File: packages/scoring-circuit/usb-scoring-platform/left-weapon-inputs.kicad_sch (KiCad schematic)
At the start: 15 parts, among them J3 LEFT WEAPON A B C, U8 SN74LVC125APWR

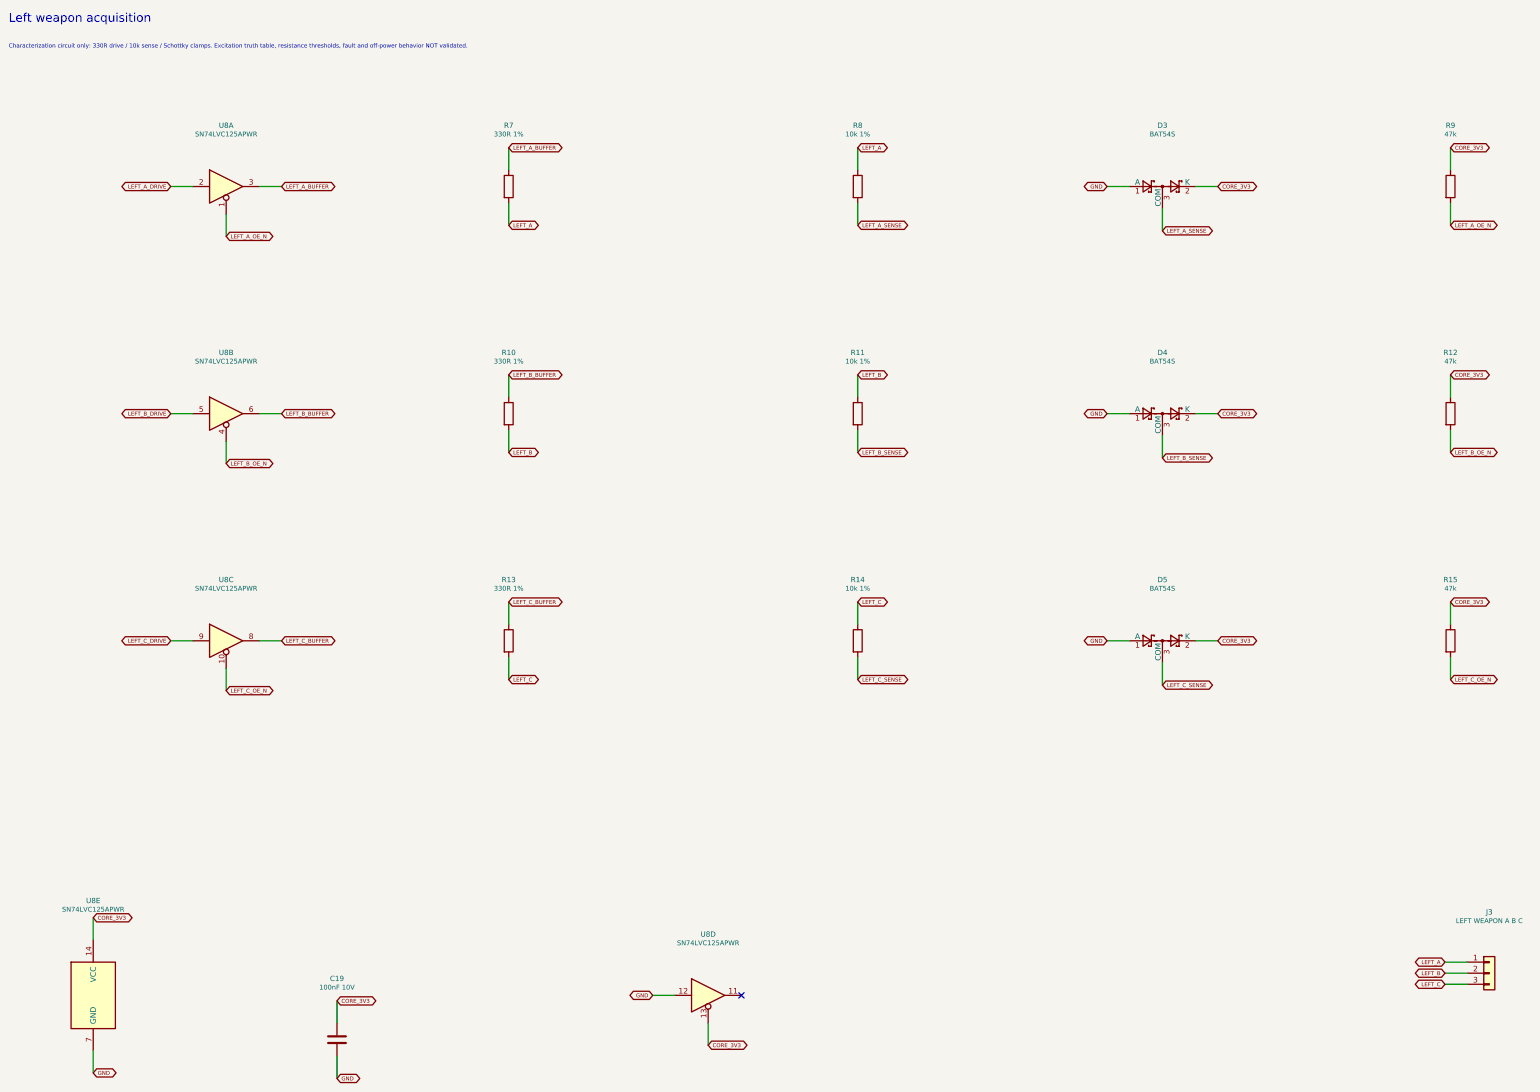
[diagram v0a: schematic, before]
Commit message: fix(scoring-circuit): strengthen STM32 sensing bias and model continuity
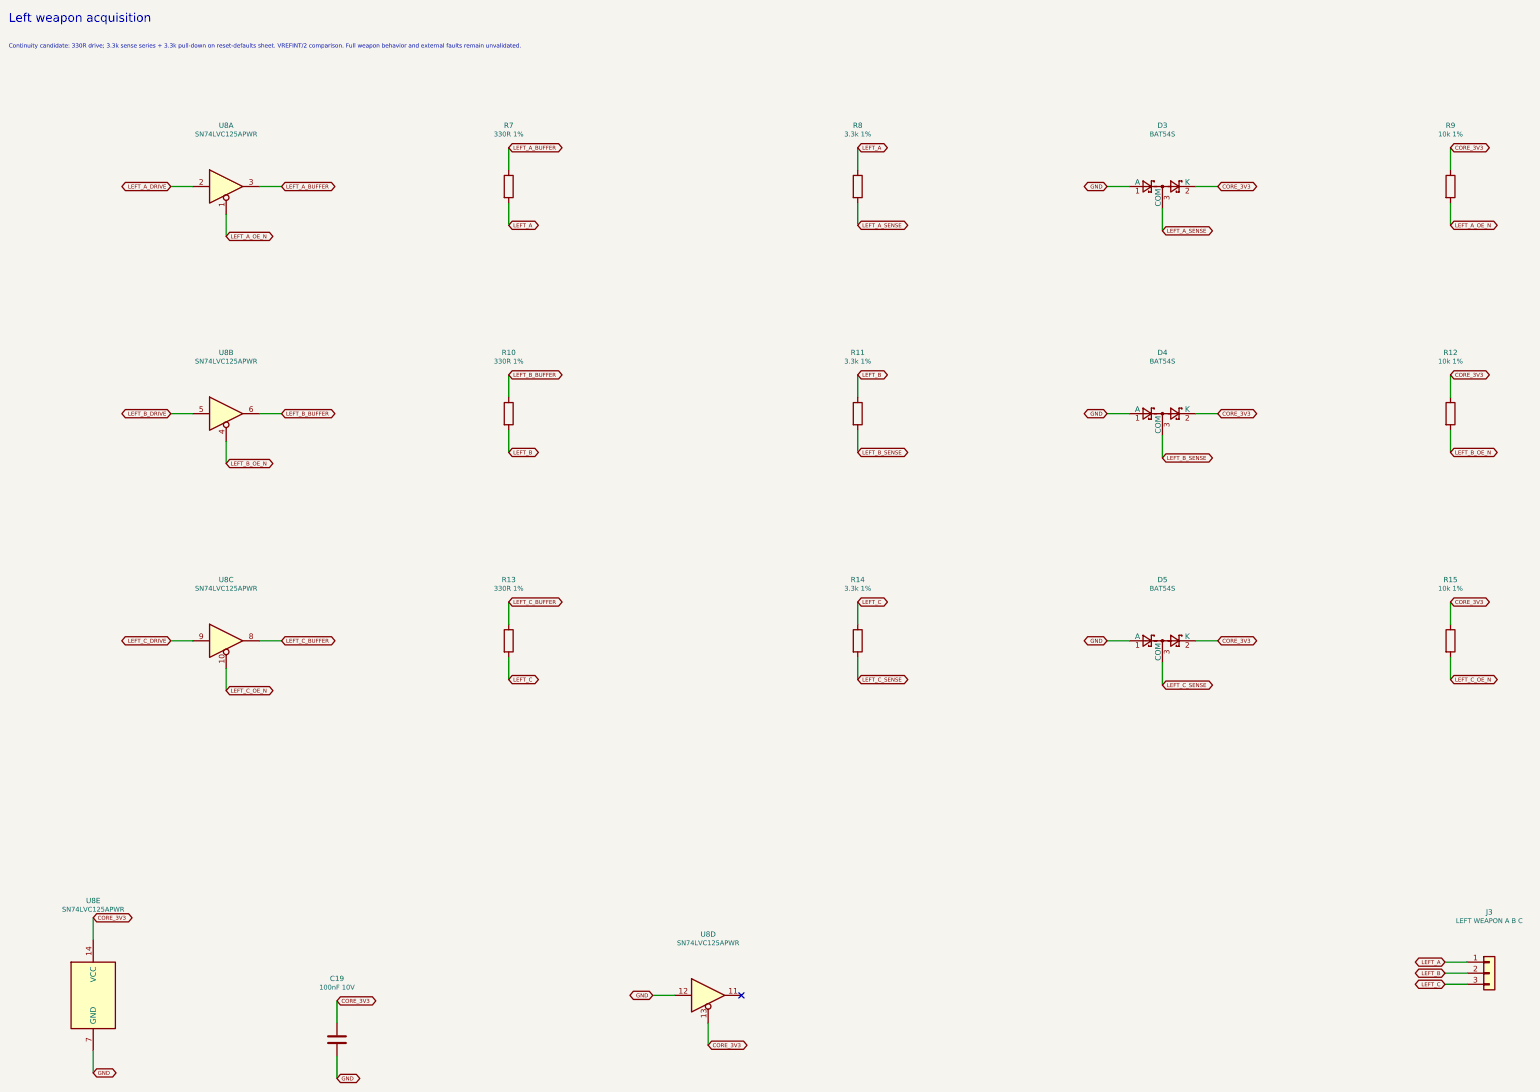
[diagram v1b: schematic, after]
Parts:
- R11, R14, R8: value 10k 1% -> 3.3k 1%
- R12, R15, R9: value 47k -> 10k 1%
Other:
- note added: "Continuity candidate: 330R drive; 3.3k sense series + 3.3k pull-down on reset-defaults sheet. VREFINT/2 comparison. Full weapon behavior and external faults remain unvalidated."
- note removed: "Characterization circuit only: 330R drive / 10k sense / Schottky clamps. Excitation truth table, resistance thresholds, fault and off-power behavior NOT validated."

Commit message: fix(scoring-circuit): improve excitation margin and power-off behavior
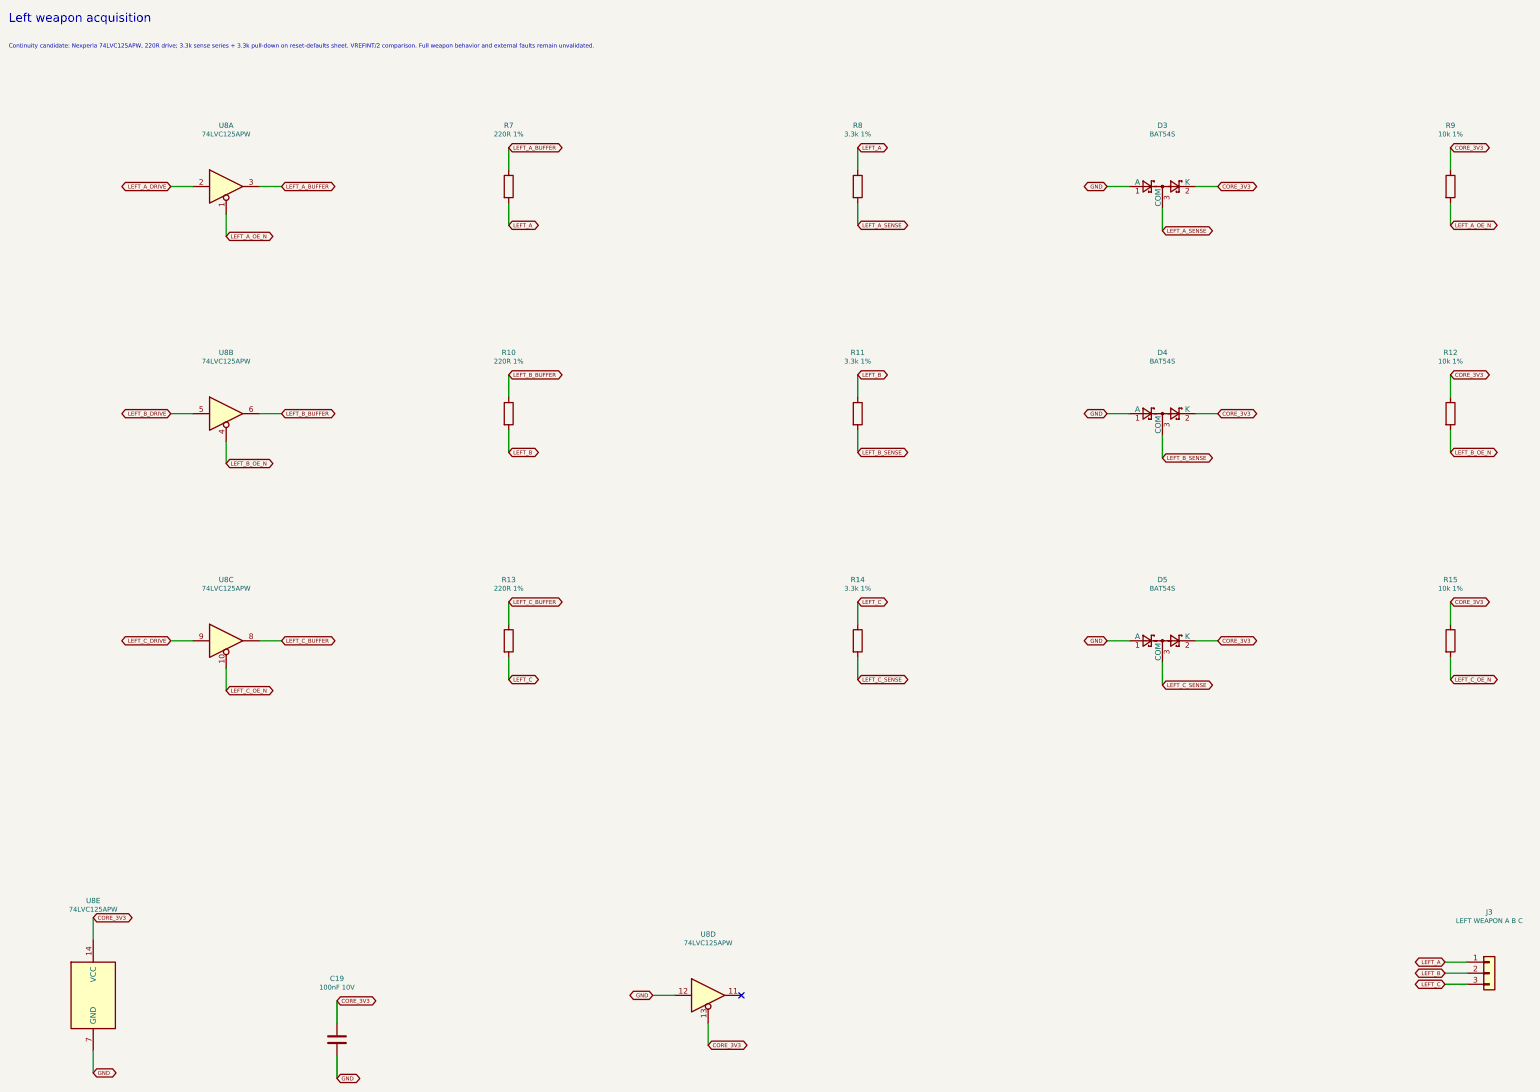
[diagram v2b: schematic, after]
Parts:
- R10, R13, R7: value 330R 1% -> 220R 1%
- U8: value SN74LVC125APWR -> 74LVC125APW; Manufacturer (none) -> Nexperia
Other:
- note added: "Continuity candidate: Nexperia 74LVC125APW, 220R drive; 3.3k sense series + 3.3k pull-down on reset-defaults sheet. VREFINT/2 comparison. Full weapon behavior and external faults remain unvalidated."
- note removed: "Continuity candidate: 330R drive; 3.3k sense series + 3.3k pull-down on reset-defaults sheet. VREFINT/2 comparison. Full weapon behavior and external faults remain unvalidated."

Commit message: feat(scoring-circuit): select exact prototype resistor parts
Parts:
- R10, R13, R7: MPN (none) -> ERJPA3F2200V; Manufacturer (none) -> Panasonic
- R11, R14, R8: MPN (none) -> RC0603FR-073K3L; Manufacturer (none) -> YAGEO
- R12, R15, R9: MPN (none) -> RC0603FR-0710KL; Manufacturer (none) -> YAGEO

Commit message: feat(scoring-circuit): select bypass and timing capacitors
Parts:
- C19: MPN (none) -> C1608X7R1H104K080AA; Manufacturer (none) -> TDK

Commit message: feat(scoring-circuit): bind diode selections and review polarity
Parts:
- D3, D4, D5: MPN (none) -> BAT54S,215; Manufacturer (none) -> Nexperia

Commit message: fix(scoring-circuit): select service headers and correct drill sizes
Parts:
- J3: footprint Connector_PinHeader_2.54mm:PinHeader_1x03_P2.54mm_Vertical -> ScoringPlatform:Samtec_HTSW-103-07-L-S; MPN (none) -> HTSW-103-07-L-S; Manufacturer (none) -> Samtec

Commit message: chore(scoring-circuit): complete assembly BOM ordering fields
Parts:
- U8: MPN (none) -> 74LVC125APW

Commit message: fix(scoring-circuit): specify orderable sensing buffers
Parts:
- U8: MPN 74LVC125APW -> 74LVC125APW,118
